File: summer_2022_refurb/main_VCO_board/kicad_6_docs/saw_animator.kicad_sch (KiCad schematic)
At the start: 25 parts

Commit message: Main VCO progress
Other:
- title: (none) -> Josh Ox Ribon Synth Main VCO board
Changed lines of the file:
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@@
 (kicad_sch (version 20211123) (generator eeschema)
   (paper "A4")
+  (title_block
+    (title "Josh Ox Ribon Synth Main VCO board")
+    (date "2022-06-18")
+    (rev "0")
+    (comment 2 "creativecommons.org/licences/by/4.0")
+    (comment 3 "license: CC by 4.0")
+    (comment 4 "Author: Jordan Acete")
+  )
   (junction (at 31.75 172.72) (diameter 0) (color 0 0 0 0)
   )

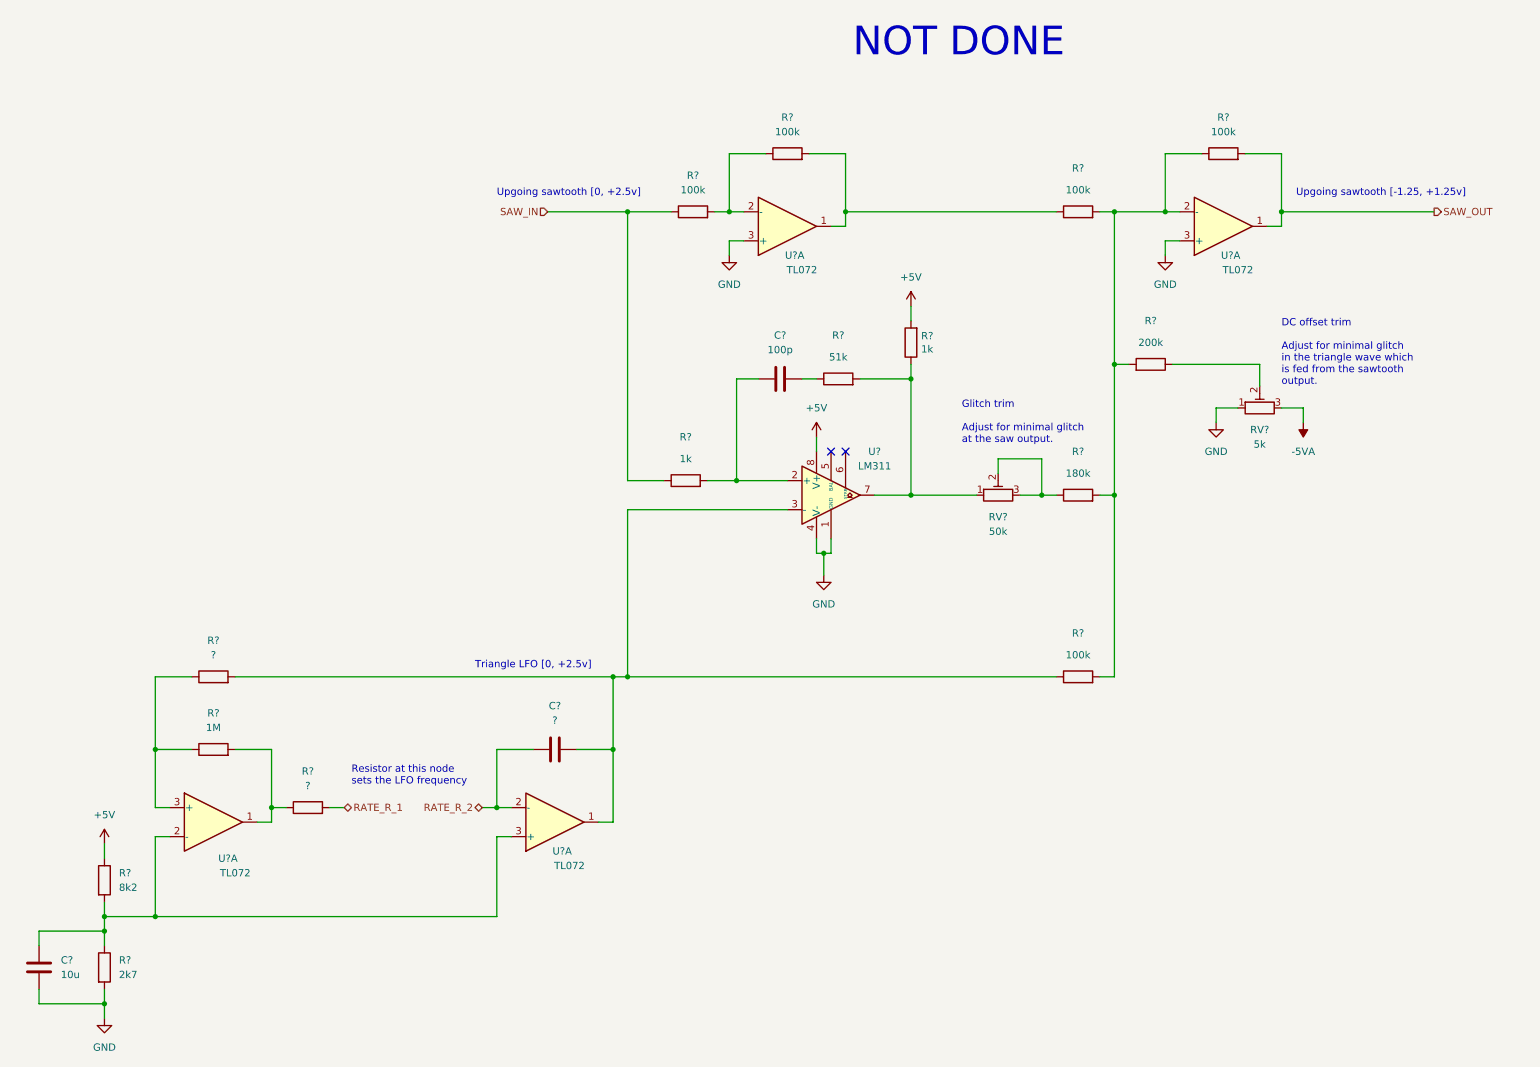
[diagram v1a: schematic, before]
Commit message: Progress on main VCO, schem getting close but not done
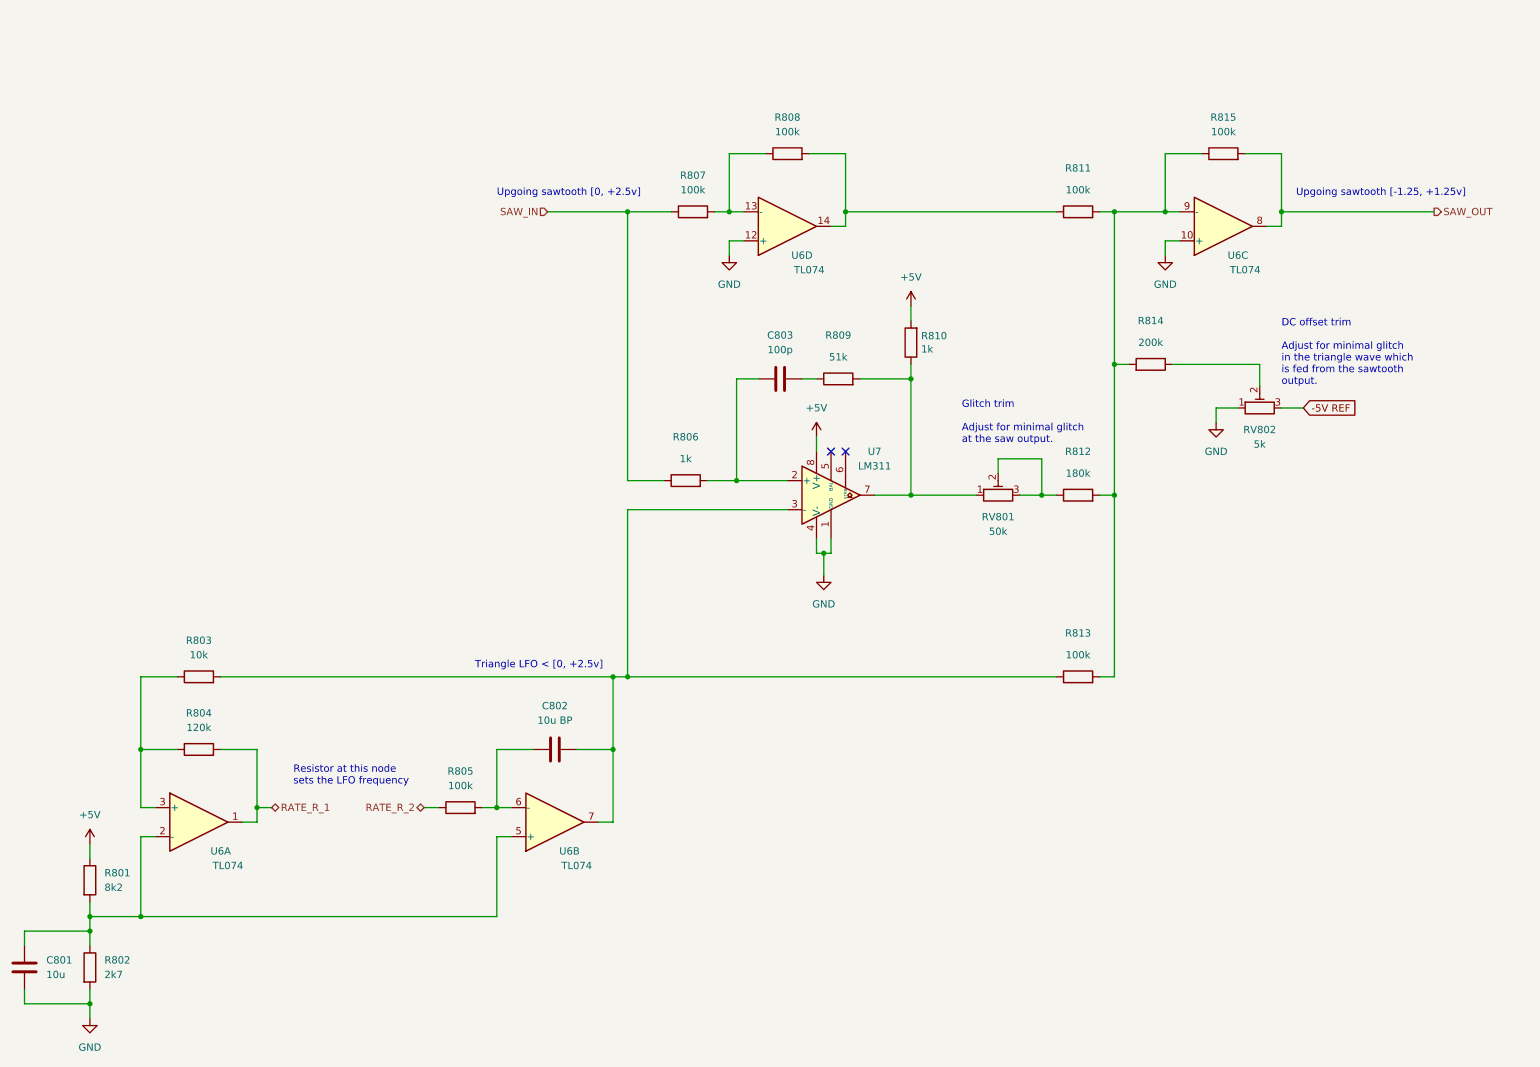
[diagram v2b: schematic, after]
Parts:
- removed U? (x4): TL072, symbol Amplifier_Operational:TL072
- added U6: TL074, symbol Amplifier_Operational:TL074
- C802: renamed from C?; value ? -> 10u BP
- R803: renamed from R?; value ? -> 10k
- R804: renamed from R?; value 1M -> 120k
- R805: renamed from R?; value ? -> 100k
- gave numbers to parts that had none: 17
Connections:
- net GND: now also U6.10 (+), U6.12 (+)
- net RATE_R_1: now also R804.2, U6.1; no longer R805.2
- net RATE_R_2: now also R805.1; no longer C802.1
- net SAW_OUT: now also U6.8
- net at C802.2, R803.2, R813.1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: now also U6.7
- net at R811.2, R812.2, R813.2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: now also U6.9 (-)
- net at R807.2, R808.1: now also U6.13 (-)
- net at R808.2, R811.1: now also U6.14
- net at R803.1, R804.1: now also U6.3 (+)
- net at C801.1, R801.2, R802.1: now also U6.2 (-), U6.5 (+)
- net -5VA renamed -5V REF
- new net: C802.1, R805.2, U6.6 (-)
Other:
- note added: "Triangle LFO < [0, +2.5v]"
- note removed: "NOT DONE"
- note removed: "Triangle LFO [0, +2.5v]"
- moved on the sheet: C801, R801, R802, R803, R804, R805

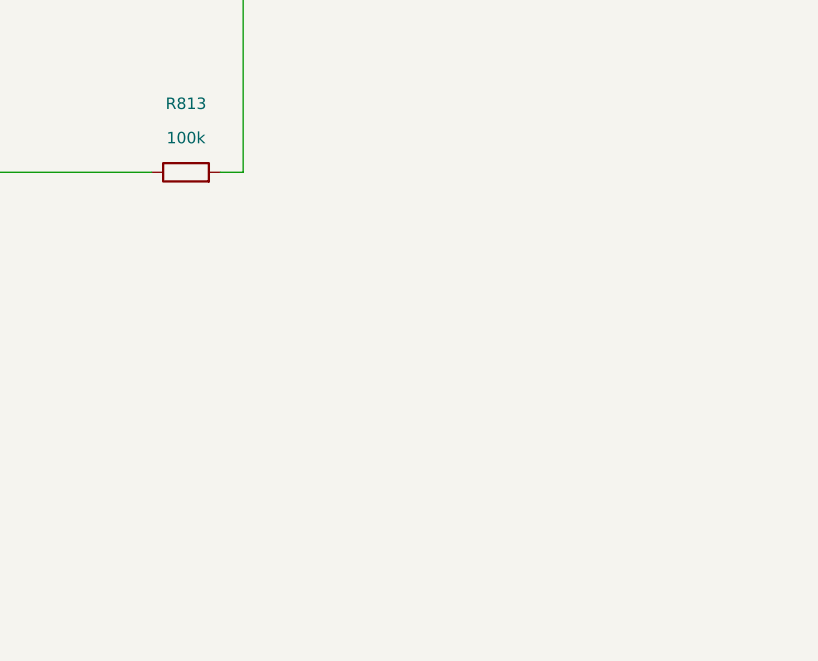
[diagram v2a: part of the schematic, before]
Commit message: Main VCO rough parts placement
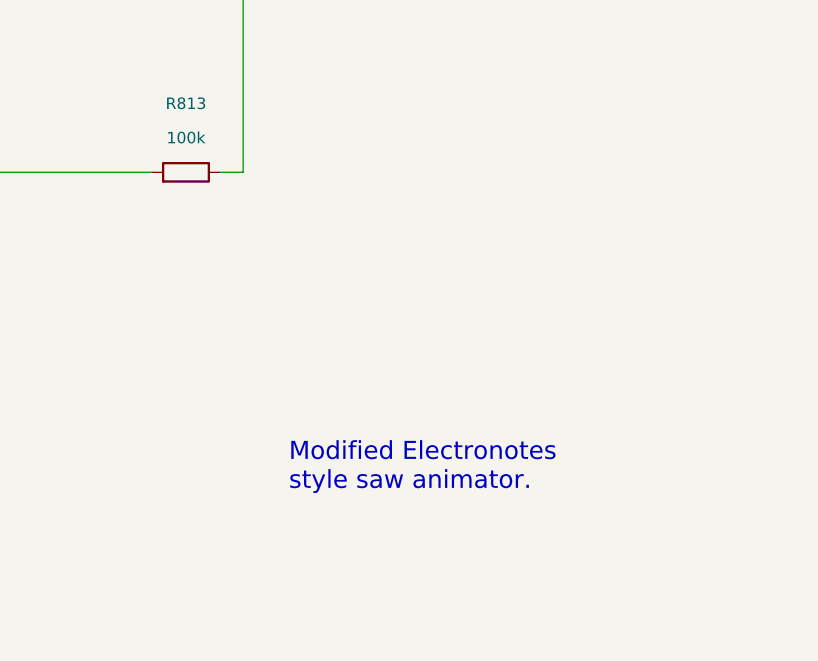
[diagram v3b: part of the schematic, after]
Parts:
- C801, C803: footprint (none) -> Capacitor_SMD:C_0805_2012Metric
- C802: footprint (none) -> Capacitor_THT:C_Radial_D6.3mm_H5.0mm_P2.50mm
- R801, R802, R803, R804, R805, R806, R807, R808, R809, R810, R811, R812, R813, R814, R815: footprint (none) -> Resistor_SMD:R_0805_2012Metric
- RV801, RV802: footprint (none) -> Potentiometer_THT:Potentiometer_Bourns_3296W_Vertical
- U6: footprint (none) -> Package_SO:SOIC-14_3.9x8.7mm_P1.27mm
- U7: footprint (none) -> Package_SO:SOIC-8_3.9x4.9mm_P1.27mm
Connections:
- net at C802.2, R803.2, U6.7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: now also R813.2; no longer R813.1
- net at R811.2, R812.2, R814.2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: now also R813.1; no longer R813.2
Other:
- note added: "Modified Electronotes style saw animator."
- moved on the sheet: R813
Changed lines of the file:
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@@
     (effects (font (size 1.27 1.27)) (justify left bottom))
+  )
+  (text "Modified Electronotes\nstyle saw animator." (at 213.36 163.83 0)
+    (effects (font (size 2 2)) (justify left bottom))
   )
   (text "Resistor at this node\nsets the LFO frequency" (at 64.77 147.32 0)
@@
     (effects (font (size 1.27 1.27)) (justify right))
   )
-  (symbol (lib_id "Device:R") (at 201.93 128.27 90) (unit 1)
+  (symbol (lib_id "Device:R") (at 201.93 128.27 270) (mirror x) (unit 1)
     (in_bom yes) (on_board yes)
     (property "Reference" "R813" (id 0) (at 201.93 120.65 90))
     (property "Value" "100k" (id 1) (at 201.93 124.46 90))
-    (property "Footprint" "" (id 2) (at 201.93 130.048 90)
+    (property "Footprint" "Resistor_SMD:R_0805_2012Metric" (id 2) (at 201.93 130.048 90)
       (effects (font (size 1.27 1.27)) hide)
     )
@@
     (property "Reference" "R808" (id 0) (at 151.13 30.48 90))
     (property "Value" "100k" (id 1) (at 151.13 33.02 90))
-    (property "Footprint" "" (id 2) (at 151.13 38.608 90)
+    (property "Footprint" "Resistor_SMD:R_0805_2012Metric" (id 2) (at 151.13 38.608 90)
       (effects (font (size 1.27 1.27)) hide)
     )
@@
     (property "Reference" "R803" (id 0) (at 48.26 121.92 90))
     (property "Value" "10k" (id 1) (at 48.26 124.46 90))
-    (property "Footprint" "" (id 2) (at 48.26 130.048 90)
+    (property "Footprint" "Resistor_SMD:R_0805_2012Metric" (id 2) (at 48.26 130.048 90)
       (effects (font (size 1.27 1.27)) hide)
     )
@@
     (property "Reference" "R806" (id 0) (at 133.35 86.36 90))
     (property "Value" "1k" (id 1) (at 133.35 90.17 90))
-    (property "Footprint" "" (id 2) (at 133.35 95.758 90)
+    (property "Footprint" "Resistor_SMD:R_0805_2012Metric" (id 2) (at 133.35 95.758 90)
       (effects (font (size 1.27 1.27)) hide)
     )
@@
       (effects (font (size 1.27 1.27)) (justify left))
     )
-    (property "Footprint" "" (id 2) (at 27.432 179.07 90)
+    (property "Footprint" "Resistor_SMD:R_0805_2012Metric" (id 2) (at 27.432 179.07 90)
       (effects (font (size 1.27 1.27)) hide)
     )
@@
     (property "Reference" "U6" (id 0) (at 153.67 54.61 0))
     (property "Value" "TL074" (id 1) (at 154.94 57.15 0))
-    (property "Footprint" "" (id 2) (at 149.86 52.07 0)
+    (property "Footprint" "Package_SO:SOIC-14_3.9x8.7mm_P1.27mm" (id 2) (at 149.86 52.07 0)
       (effects (font (size 1.27 1.27)) hide)
     )
@@
     (property "Reference" "R805" (id 0) (at 93.98 144.78 90))
     (property "Value" "100k" (id 1) (at 93.98 147.32 90))
-    (property "Footprint" "" (id 2) (at 93.98 152.908 90)
+    (property "Footprint" "Resistor_SMD:R_0805_2012Metric" (id 2) (at 93.98 152.908 90)
       (effects (font (size 1.27 1.27)) hide)
     )
@@
     (property "Reference" "R815" (id 0) (at 227.33 30.48 90))
     (property "Value" "100k" (id 1) (at 227.33 33.02 90))
-    (property "Footprint" "" (id 2) (at 227.33 38.608 90)
+    (property "Footprint" "Resistor_SMD:R_0805_2012Metric" (id 2) (at 227.33 38.608 90)
       (effects (font (size 1.27 1.27)) hide)
     )
@@
     (property "Reference" "R812" (id 0) (at 201.93 88.9 90))
     (property "Value" "180k" (id 1) (at 201.93 92.71 90))
-    (property "Footprint" "" (id 2) (at 201.93 98.298 90)
+    (property "Footprint" "Resistor_SMD:R_0805_2012Metric" (id 2) (at 201.93 98.298 90)
       (effects (font (size 1.27 1.27)) hide)
     )
@@
     (property "Reference" "R807" (id 0) (at 134.62 40.64 90))
     (property "Value" "100k" (id 1) (at 134.62 43.18 90))
-    (property "Footprint" "" (id 2) (at 134.62 48.768 90)
+    (property "Footprint" "Resistor_SMD:R_0805_2012Metric" (id 2) (at 134.62 48.768 90)
       (effects (font (size 1.27 1.27)) hide)
     )
@@
     (property "Reference" "U6" (id 0) (at 52.07 158.75 0))
     (property "Value" "TL074" (id 1) (at 53.34 161.29 0))
-    (property "Footprint" "" (id 2) (at 46.99 151.13 0)
+    (property "Footprint" "Package_SO:SOIC-14_3.9x8.7mm_P1.27mm" (id 2) (at 46.99 151.13 0)
       (effects (font (size 1.27 1.27)) hide)
     )
@@
     (property "Reference" "R811" (id 0) (at 201.93 39.37 90))
     (property "Value" "100k" (id 1) (at 201.93 43.18 90))
-    (property "Footprint" "" (id 2) (at 201.93 48.768 90)
+    (property "Footprint" "Resistor_SMD:R_0805_2012Metric" (id 2) (at 201.93 48.768 90)
       (effects (font (size 1.27 1.27)) hide)
     )
@@
     (property "Reference" "RV802" (id 0) (at 233.68 85.09 90))
     (property "Value" "5k" (id 1) (at 233.68 87.63 90))
-    (property "Footprint" "" (id 2) (at 233.68 81.28 0)
+    (property "Footprint" "Potentiometer_THT:Potentiometer_Bourns_3296W_Vertical" (id 2) (at 233.68 81.28 0)
       (effects (font (size 1.27 1.27)) hide)
     )
@@
     (property "Reference" "R804" (id 0) (at 48.26 134.62 90))
     (property "Value" "120k" (id 1) (at 48.26 137.16 90))
-    (property "Footprint" "" (id 2) (at 48.26 142.748 90)
+    (property "Footprint" "Resistor_SMD:R_0805_2012Metric" (id 2) (at 48.26 142.748 90)
       (effects (font (size 1.27 1.27)) hide)
     )
@@
       (effects (font (size 1.27 1.27)) (justify left))
     )
-    (property "Footprint" "" (id 2) (at 27.432 163.83 90)
+    (property "Footprint" "Resistor_SMD:R_0805_2012Metric" (id 2) (at 27.432 163.83 90)
       (effects (font (size 1.27 1.27)) hide)
     )
@@
     (property "Reference" "R809" (id 0) (at 160.02 68.58 90))
     (property "Value" "51k" (id 1) (at 160.02 72.39 90))
-    (property "Footprint" "" (id 2) (at 160.02 77.978 90)
+    (property "Footprint" "Resistor_SMD:R_0805_2012Metric" (id 2) (at 160.02 77.978 90)
       (effects (font (size 1.27 1.27)) hide)
     )
@@
     (property "Reference" "C803" (id 0) (at 149.86 68.58 90))
     (property "Value" "100p" (id 1) (at 149.86 71.12 90))
-    (property "Footprint" "" (id 2) (at 153.67 75.2348 0)
+    (property "Footprint" "Capacitor_SMD:C_0805_2012Metric" (id 2) (at 153.67 75.2348 0)
       (effects (font (size 1.27 1.27)) hide)
     )
@@
     (property "Reference" "U7" (id 0) (at 166.37 88.9 0))
     (property "Value" "LM311" (id 1) (at 166.37 91.44 0))
-    (property "Footprint" "" (id 2) (at 158.75 96.52 0)
+    (property "Footprint" "Package_SO:SOIC-8_3.9x4.9mm_P1.27mm" (id 2) (at 158.75 96.52 0)
       (effects (font (size 1.27 1.27)) hide)
     )
@@
       (effects (font (size 1.27 1.27)) (justify left))
     )
-    (property "Footprint" "" (id 2) (at 18.7452 182.88 0)
+    (property "Footprint" "Capacitor_SMD:C_0805_2012Metric" (id 2) (at 18.7452 182.88 0)
       (effects (font (size 1.27 1.27)) hide)
     )
@@
     (property "Reference" "R814" (id 0) (at 214.63 66.04 90))
     (property "Value" "200k" (id 1) (at 214.63 69.85 90))
-    (property "Footprint" "" (id 2) (at 214.63 75.438 90)
+    (property "Footprint" "Resistor_SMD:R_0805_2012Metric" (id 2) (at 214.63 75.438 90)
       (effects (font (size 1.27 1.27)) hide)
     )
@@
     (property "Reference" "C802" (id 0) (at 110.49 133.35 90))
     (property "Value" "10u BP" (id 1) (at 110.49 135.89 90))
-    (property "Footprint" "" (id 2) (at 114.3 140.0048 0)
+    (property "Footprint" "Capacitor_THT:C_Radial_D6.3mm_H5.0mm_P2.50mm" (id 2) (at 114.3 140.0048 0)
       (effects (font (size 1.27 1.27)) hide)
     )
@@
     (property "Reference" "U6" (id 0) (at 229.87 54.61 0))
     (property "Value" "TL074" (id 1) (at 231.14 57.15 0))
-    (property "Footprint" "" (id 2) (at 226.06 52.07 0)
+    (property "Footprint" "Package_SO:SOIC-14_3.9x8.7mm_P1.27mm" (id 2) (at 226.06 52.07 0)
       (effects (font (size 1.27 1.27)) hide)
     )
@@
       (effects (font (size 1.27 1.27)) (justify right))
     )
-    (property "Footprint" "" (id 2) (at 174.498 69.85 90)
+    (property "Footprint" "Resistor_SMD:R_0805_2012Metric" (id 2) (at 174.498 69.85 90)
       (effects (font (size 1.27 1.27)) hide)
     )
@@
     (property "Reference" "RV801" (id 0) (at 187.96 100.33 90))
     (property "Value" "50k" (id 1) (at 187.96 102.87 90))
-    (property "Footprint" "" (id 2) (at 187.96 96.52 0)
+    (property "Footprint" "Potentiometer_THT:Potentiometer_Bourns_3296W_Vertical" (id 2) (at 187.96 96.52 0)
       (effects (font (size 1.27 1.27)) hide)
     )
@@
     (property "Reference" "U6" (id 0) (at 113.03 158.75 0))
     (property "Value" "TL074" (id 1) (at 114.3 161.29 0))
-    (property "Footprint" "" (id 2) (at 109.22 156.21 0)
-      (effects (font (size 1.27 1.27)) hide)
-    )
+    (property "Footprint" "Package_SO:SOIC-14_3.9x8.7mm_P1.27mm" (id 2) (at 109.22 156.21 0)
+      (effects (font (size 1.27 1.27)) hide)
+    )
